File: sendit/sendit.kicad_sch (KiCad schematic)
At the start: 7 parts, among them J1 Conn_01x03

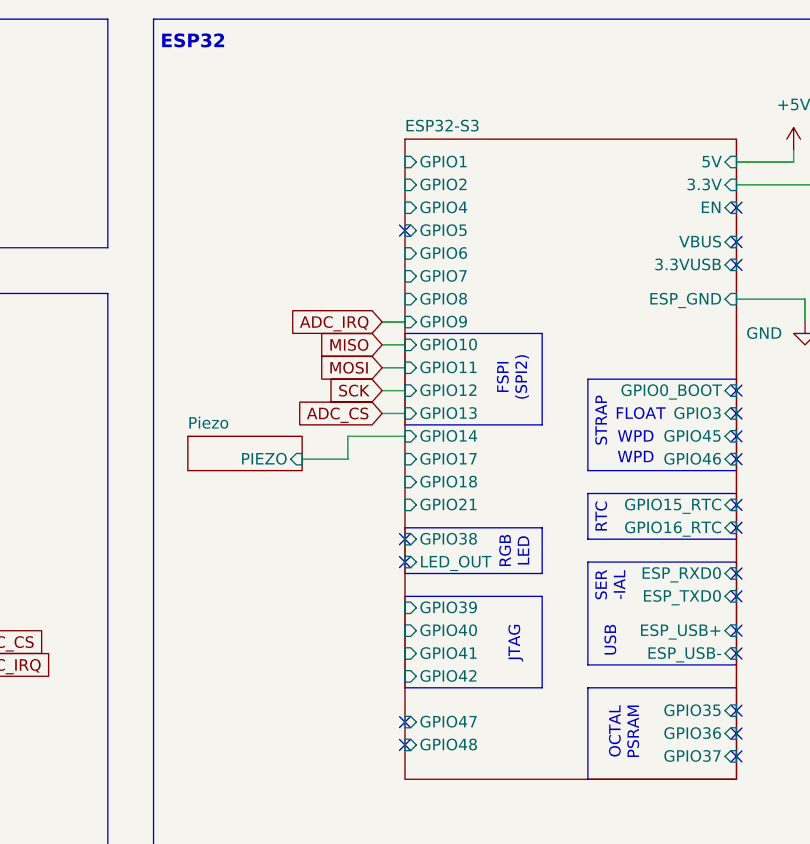
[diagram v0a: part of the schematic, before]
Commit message: passing erc and drc
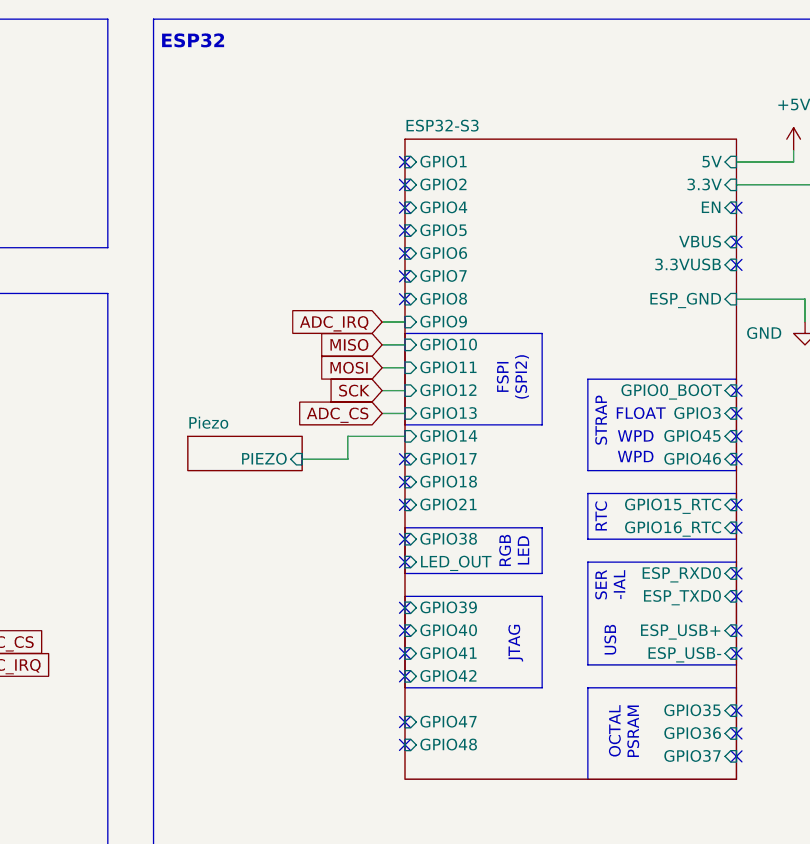
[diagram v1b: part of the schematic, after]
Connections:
- no-connect marks 23 -> 36
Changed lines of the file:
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@@
+	)
+	(no_connect
+		(at 157.48 101.6)
 	)
 	(no_connect
 		(at 194.31 72.39)
+	)
+	(no_connect
+		(at 157.48 80.01)
 	)
 	(no_connect
@@
 	)
 	(no_connect
+		(at 157.48 96.52)
+	)
+	(no_connect
 		(at 194.31 95.25)
 	)
@@
 	)
 	(no_connect
+		(at 157.48 104.14)
+	)
+	(no_connect
 		(at 194.31 55.88)
 	)
 	(no_connect
 		(at 194.31 101.6)
+	)
+	(no_connect
+		(at 157.48 57.15)
+	)
+	(no_connect
+		(at 157.48 52.07)
 	)
 	(no_connect
@@
 	(no_connect
 		(at 44.45 44.45)
+	)
+	(no_connect
+		(at 157.48 46.99)
+	)
+	(no_connect
+		(at 157.48 62.23)
+	)
+	(no_connect
+		(at 157.48 85.09)
 	)
 	(no_connect
@@
 	)
 	(no_connect
+		(at 157.48 99.06)
+	)
+	(no_connect
+		(at 157.48 59.69)
+	)
+	(no_connect
 		(at 194.31 52.07)
 	)
@@
 	)
 	(no_connect
+		(at 157.48 49.53)
+	)
+	(no_connect
 		(at 157.48 109.22)
 	)
+	(no_connect
+		(at 157.48 82.55)
+	)
 	(wire

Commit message: silkscreen updated, looking good.
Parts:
- INPUT1: value Conn_01x03 -> Conn_01x02; footprint Connector_Phoenix_MC:PhoenixContact_MC_1,5_2-G-3.5_1x02_P3.50mm_Horizontal -> yarrboard:PhoenixContact_MC_1,5_2-G-3.5_1x02_P3.50mm_Horizontal
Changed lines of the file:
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@@
 			)
 		)
-		(property "Value" "Conn_01x03"
+		(property "Value" "Conn_01x02"
 			(at 52.07 38.1 0)
 			(effects
@@
 			)
 		)
-		(property "Footprint" "Connector_Phoenix_MC:PhoenixContact_MC_1,5_2-G-3.5_1x02_P3.50mm_Horizontal"
+		(property "Footprint" "yarrboard:PhoenixContact_MC_1,5_2-G-3.5_1x02_P3.50mm_Horizontal"
 			(at 52.07 44.45 0)
 			(effects

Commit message: bom and placement looking good.
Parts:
- J1: value Conn_01x03 -> Conn_01x02

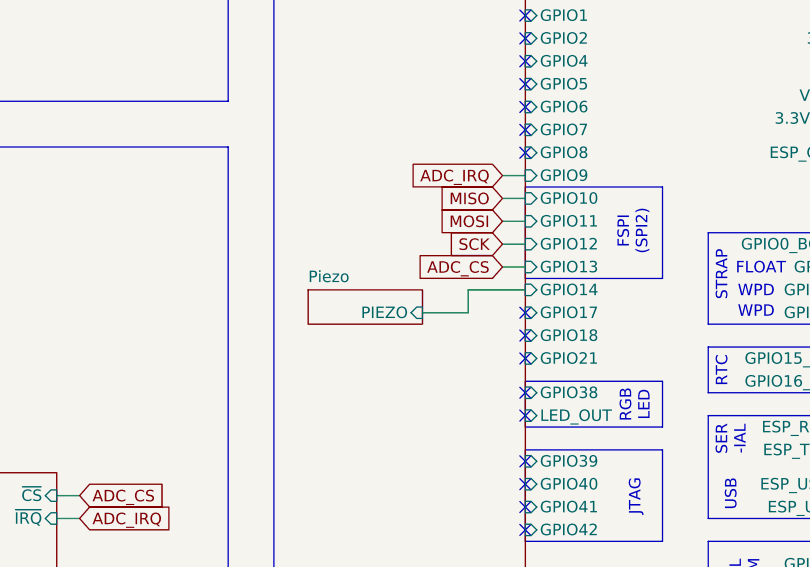
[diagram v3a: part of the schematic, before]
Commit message: some final resistor value tweaking
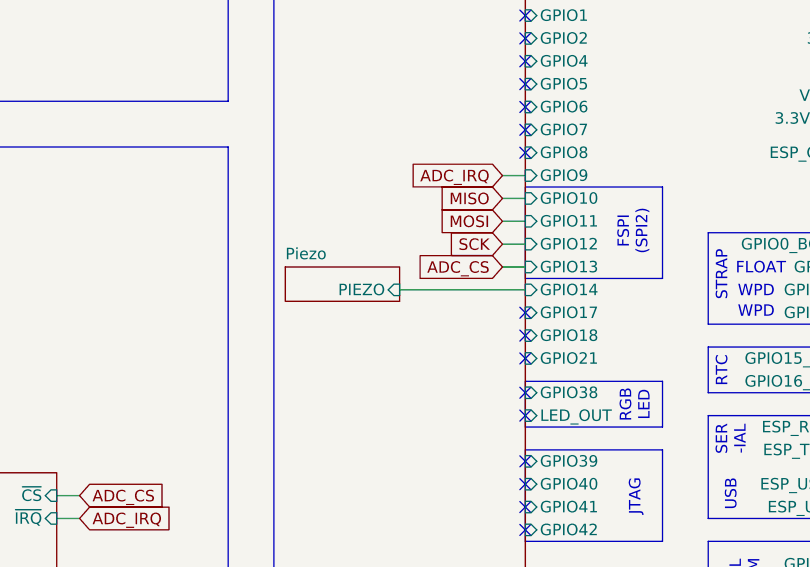
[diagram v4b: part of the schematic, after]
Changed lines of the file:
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@@
-	(wire
-		(pts
-			(xy 151.13 77.47) (xy 151.13 80.01)
-		)
-		(stroke
-			(width 0)
-			(type default)
-		)
-	)
 	(wire
 		(pts
@@
 	(wire
 		(pts
-			(xy 151.13 80.01) (xy 146.05 80.01)
+			(xy 143.51 77.47) (xy 157.48 77.47)
 		)
 		(stroke
@@
 		(pts
 			(xy 201.93 62.23) (xy 201.93 64.77)
-		)
-		(stroke
-			(width 0)
-			(type default)
-		)
-	)
-	(wire
-		(pts
-			(xy 157.48 77.47) (xy 151.13 77.47)
 		)
 		(stroke
@@
 	)
 	(sheet
-		(at 133.35 77.47)
+		(at 130.81 74.93)
 		(size 12.7 3.81)
 		(exclude_from_sim no)
@@
 		)
 		(property "Sheetname" "Piezo"
-			(at 133.35 76.7584 0)
+			(at 130.81 74.2184 0)
 			(effects
 				(font
@@
 		)
 		(property "Sheetfile" "piezo.kicad_sch"
-			(at 133.35 81.8646 0)
+			(at 130.81 79.3246 0)
 			(effects
 				(font
@@
 		)
 		(pin "PIEZO" input
-			(at 146.05 80.01 0)
-			(effects
-				(font
+			(at 143.51 77.47 0)
+			(effects
+				(font

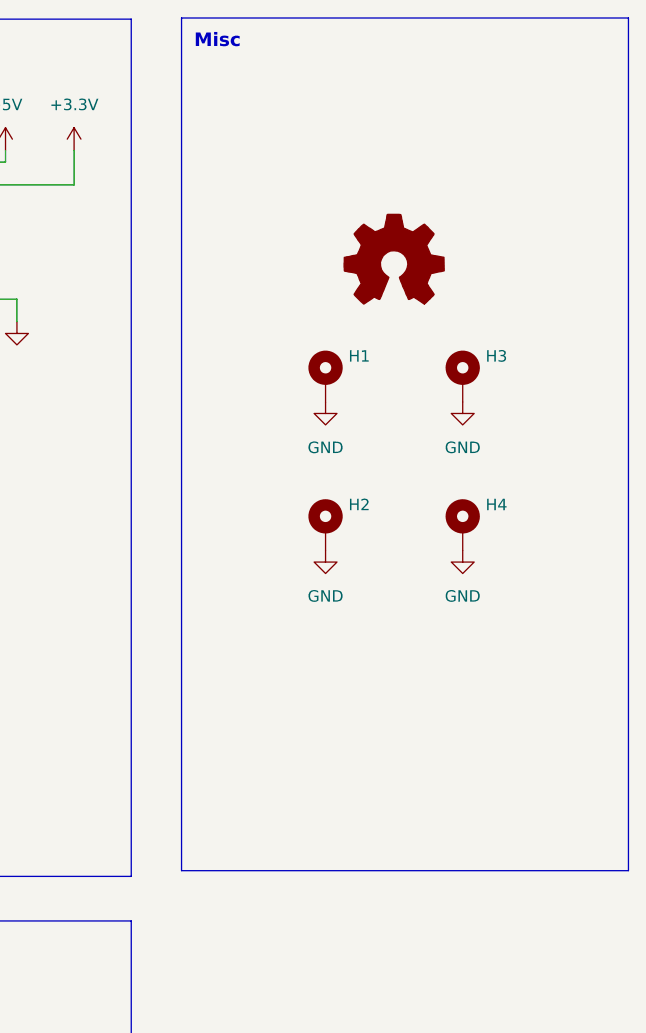
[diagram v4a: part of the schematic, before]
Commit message: cleaning up schematics a bit for design review
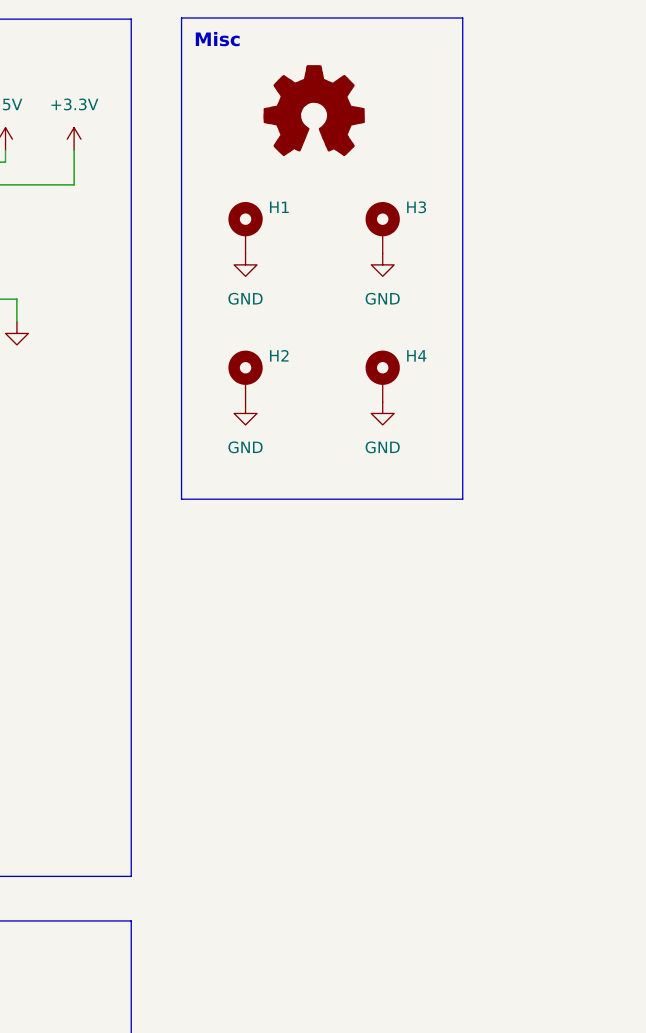
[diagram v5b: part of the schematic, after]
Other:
- title: (none) -> https://github.com/hoeken/sendit
- moved on the sheet: H1, H2, H3, H4

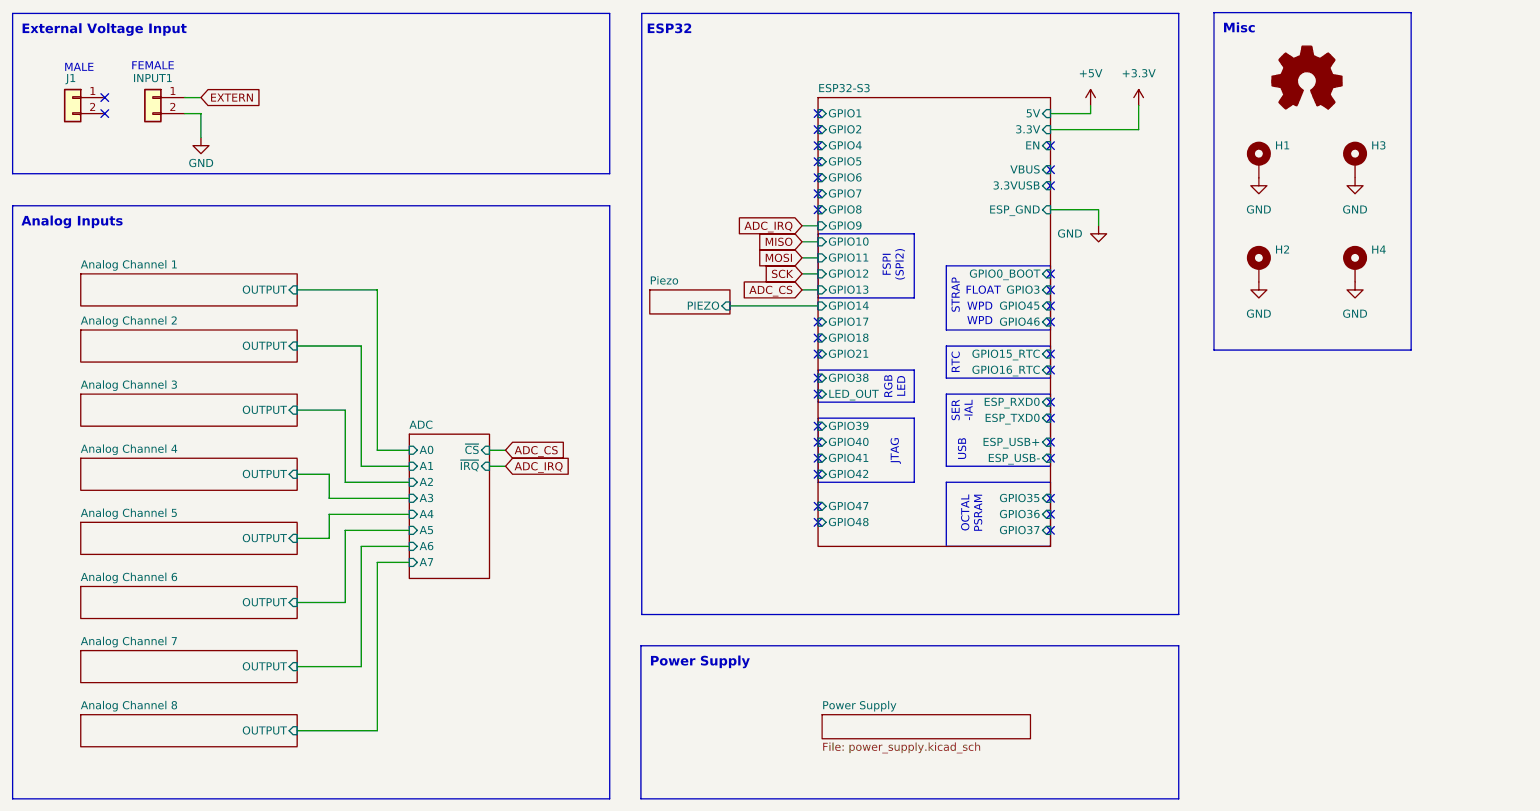
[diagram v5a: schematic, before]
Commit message: started work on the rev c schematic
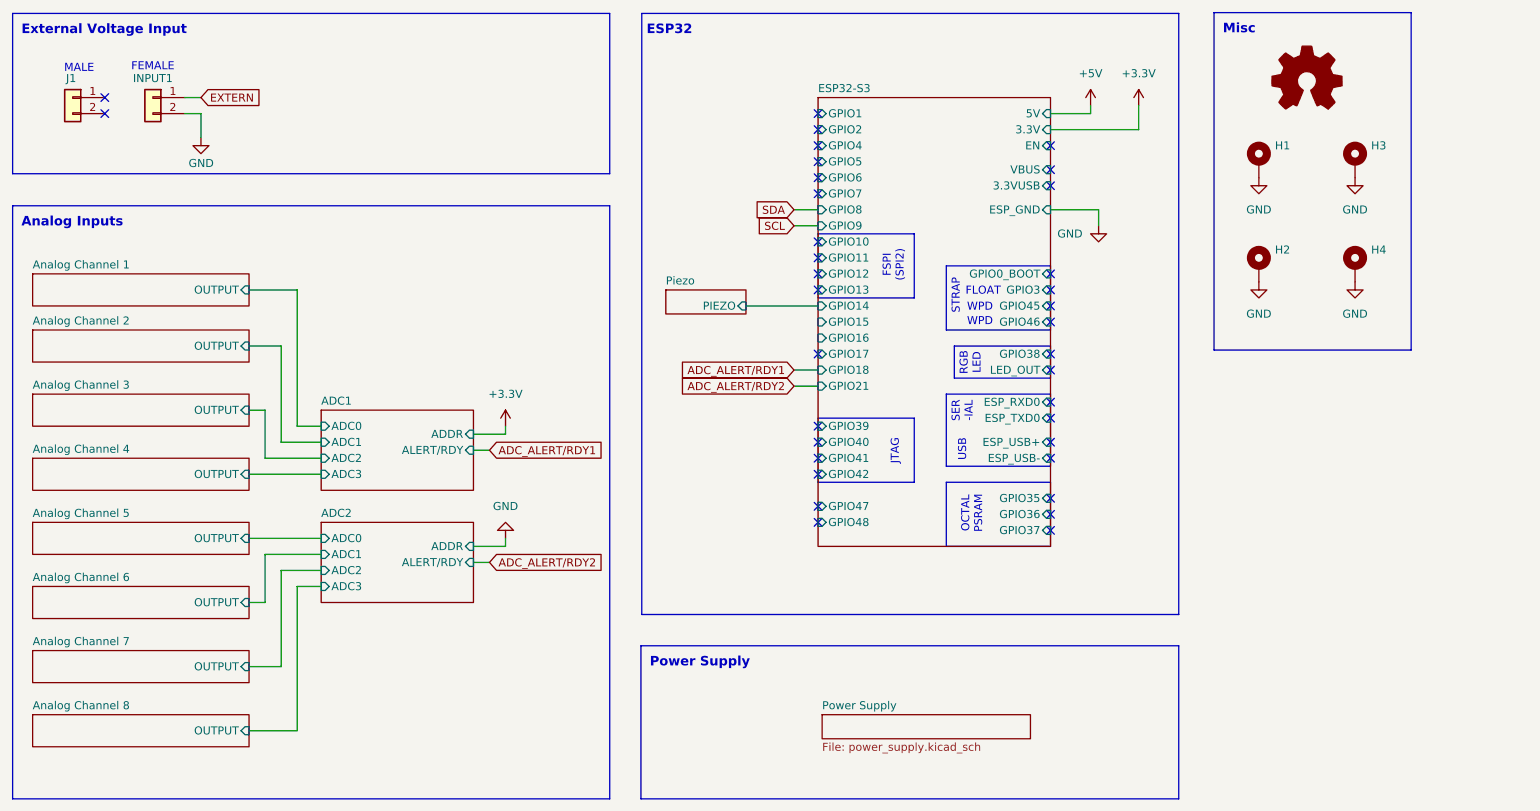
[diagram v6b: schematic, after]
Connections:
- no-connect marks 36 -> 35
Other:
- removed sheet ADC
- added sheet ADC1 (1115_adc.kicad_sch)
- added sheet ADC2 (1115_adc.kicad_sch)
- sheet ESP32-S3 ports: added GPIO15, GPIO16; removed GPIO15_RTC, GPIO16_RTC
- note removed: "RTC"

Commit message: more work on rev c board schematic
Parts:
- added TP21, TP22: ~, TestPoint:TestPoint_THTPad_D2.0mm_Drill1.0mm, symbol Connector:TestPoint
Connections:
- net SCL: now also TP22.1
- net SDA: now also TP21.1
- net EXTERN renamed VEXT

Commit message: most of the work on the schematic is done.
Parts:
- removed INPUT1: Conn_01x02, yarrboard:PhoenixContact_MC_1,5_2-G-3.5_1x02_P3.50mm_Horizontal, symbol Connector_Generic:Conn_01x02
- removed J1: Conn_01x02, symbol Connector_Generic:Conn_01x02
- renumbered LOGO2 to LOGO1, TP21 to TP1, TP22 to TP2
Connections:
- no-connect marks 35 -> 33
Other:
- note removed: "External Voltage Input"
- note removed: "FEMALE"
- note removed: "MALE"
